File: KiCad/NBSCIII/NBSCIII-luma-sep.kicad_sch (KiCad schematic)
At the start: 11 parts, among them U1 LM324N

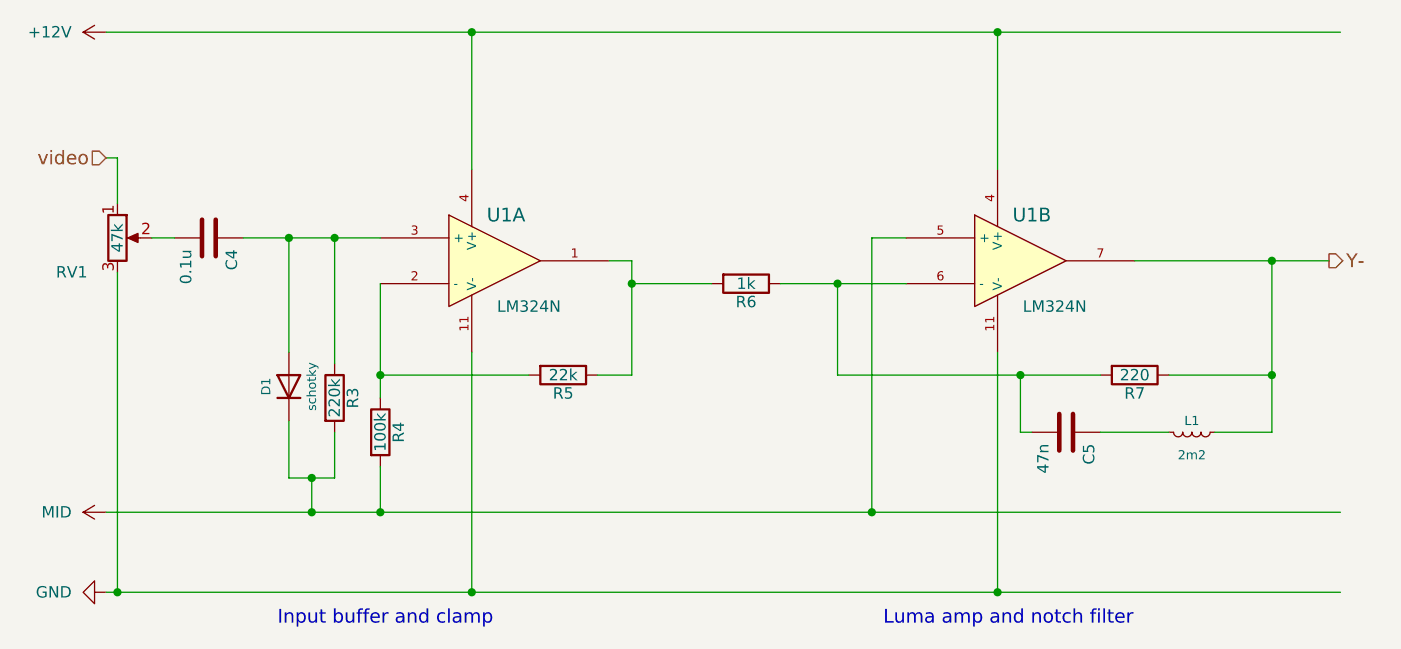
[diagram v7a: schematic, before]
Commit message: derescue lm324
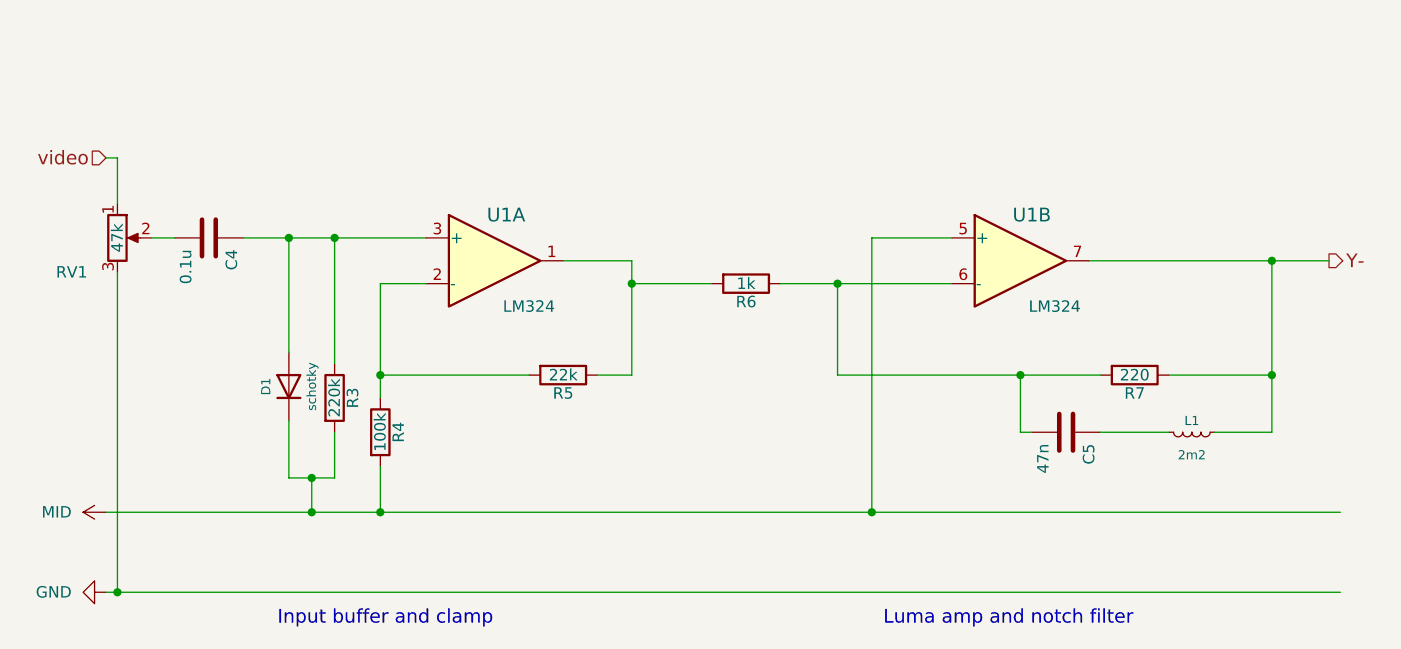
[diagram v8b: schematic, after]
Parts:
- U1: value LM324N -> LM324; symbol NBSCIII-rescue:LM324N -> Amplifier_Operational:LM324
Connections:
- net GND: no longer U1.11 (V-), U1.11 (V-)
- removed net +12V: U1.4 (V+), U1.4 (V+)
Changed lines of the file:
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@@
   (junction (at 68.58 59.69) (diameter 0) (color 0 0 0 0)
   )
-  (junction (at 142.24 36.83) (diameter 0) (color 0 0 0 0)
-  )
-  (junction (at 83.82 36.83) (diameter 0) (color 0 0 0 0)
-  )
   (junction (at 63.5 59.69) (diameter 0) (color 0 0 0 0)
   )
-  (junction (at 142.24 99.06) (diameter 0) (color 0 0 0 0)
-  )
-  (junction (at 83.82 99.06) (diameter 0) (color 0 0 0 0)
-  )
   (junction (at 66.04 90.17) (diameter 0) (color 0 0 0 0)
   )
@@
   (junction (at 66.04 86.36) (diameter 0) (color 0 0 0 0)
   )
-  (wire (pts (xy 128.27 59.69) (xy 132.08 59.69))
+  (wire (pts (xy 128.27 59.69) (xy 137.16 59.69))
     (stroke (width 0) (type default) (color 0 0 0 0))
   )
@@
     (stroke (width 0) (type default) (color 0 0 0 0))
   )
-  (wire (pts (xy 83.82 99.06) (xy 142.24 99.06))
-    (stroke (width 0) (type default) (color 0 0 0 0))
-  )
   (wire (pts (xy 68.58 59.69) (xy 68.58 73.66))
     (stroke (width 0) (type default) (color 0 0 0 0))
@@
     (stroke (width 0) (type default) (color 0 0 0 0))
   )
-  (wire (pts (xy 142.24 36.83) (xy 142.24 52.07))
-    (stroke (width 0) (type default) (color 0 0 0 0))
-  )
   (wire (pts (xy 73.66 74.93) (xy 73.66 77.47))
     (stroke (width 0) (type default) (color 0 0 0 0))
@@
     (stroke (width 0) (type default) (color 0 0 0 0))
   )
-  (wire (pts (xy 83.82 36.83) (xy 142.24 36.83))
-    (stroke (width 0) (type default) (color 0 0 0 0))
-  )
   (wire (pts (xy 128.27 90.17) (xy 128.27 59.69))
     (stroke (width 0) (type default) (color 0 0 0 0))
   )
-  (wire (pts (xy 142.24 99.06) (xy 180.34 99.06))
-    (stroke (width 0) (type default) (color 0 0 0 0))
-  )
-  (wire (pts (xy 44.45 99.06) (xy 83.82 99.06))
+  (wire (pts (xy 44.45 99.06) (xy 180.34 99.06))
     (stroke (width 0) (type default) (color 0 0 0 0))
   )
@@
     (stroke (width 0) (type default) (color 0 0 0 0))
   )
-  (wire (pts (xy 142.24 99.06) (xy 142.24 72.39))
-    (stroke (width 0) (type default) (color 0 0 0 0))
-  )
   (wire (pts (xy 63.5 59.69) (xy 68.58 59.69))
     (stroke (width 0) (type default) (color 0 0 0 0))
   )
-  (wire (pts (xy 83.82 52.07) (xy 83.82 36.83))
+  (wire (pts (xy 73.66 64.77) (xy 78.74 64.77))
     (stroke (width 0) (type default) (color 0 0 0 0))
   )
@@
     (stroke (width 0) (type default) (color 0 0 0 0))
   )
-  (wire (pts (xy 43.18 36.83) (xy 83.82 36.83))
-    (stroke (width 0) (type default) (color 0 0 0 0))
-  )
   (wire (pts (xy 101.6 64.77) (xy 101.6 74.93))
     (stroke (width 0) (type default) (color 0 0 0 0))
   )
-  (wire (pts (xy 157.48 62.23) (xy 172.72 62.23))
-    (stroke (width 0) (type default) (color 0 0 0 0))
-  )
   (wire (pts (xy 144.78 74.93) (xy 153.67 74.93))
     (stroke (width 0) (type default) (color 0 0 0 0))
@@
     (stroke (width 0) (type default) (color 0 0 0 0))
   )
-  (wire (pts (xy 142.24 36.83) (xy 180.34 36.83))
-    (stroke (width 0) (type default) (color 0 0 0 0))
-  )
   (wire (pts (xy 144.78 81.28) (xy 146.05 81.28))
     (stroke (width 0) (type default) (color 0 0 0 0))
@@
     (stroke (width 0) (type default) (color 0 0 0 0))
   )
-  (wire (pts (xy 68.58 59.69) (xy 73.66 59.69))
+  (wire (pts (xy 68.58 59.69) (xy 78.74 59.69))
+    (stroke (width 0) (type default) (color 0 0 0 0))
+  )
+  (wire (pts (xy 124.46 64.77) (xy 137.16 64.77))
     (stroke (width 0) (type default) (color 0 0 0 0))
   )
@@
     (stroke (width 0) (type default) (color 0 0 0 0))
   )
+  (wire (pts (xy 152.4 62.23) (xy 172.72 62.23))
+    (stroke (width 0) (type default) (color 0 0 0 0))
+  )
   (wire (pts (xy 172.72 81.28) (xy 172.72 74.93))
     (stroke (width 0) (type default) (color 0 0 0 0))
@@
     (stroke (width 0) (type default) (color 0 0 0 0))
   )
-  (wire (pts (xy 132.08 64.77) (xy 124.46 64.77))
-    (stroke (width 0) (type default) (color 0 0 0 0))
-  )
   (wire (pts (xy 144.78 81.28) (xy 144.78 74.93))
     (stroke (width 0) (type default) (color 0 0 0 0))
@@
     (stroke (width 0) (type default) (color 0 0 0 0))
   )
-  (wire (pts (xy 83.82 72.39) (xy 83.82 99.06))
-    (stroke (width 0) (type default) (color 0 0 0 0))
-  )
   (wire (pts (xy 172.72 74.93) (xy 172.72 62.23))
     (stroke (width 0) (type default) (color 0 0 0 0))
@@
     (stroke (width 0) (type default) (color 0 0 0 0))
   )
-  (wire (pts (xy 99.06 62.23) (xy 101.6 62.23))
+  (wire (pts (xy 93.98 62.23) (xy 101.6 62.23))
     (stroke (width 0) (type default) (color 0 0 0 0))
   )
@@
     (effects (font (size 1.524 1.524)) (justify left))
   )
-  (symbol (lib_id "NBSCIII-rescue:LM324N") (at 86.36 62.23 0) (unit 1)
+  (symbol (lib_id "Amplifier_Operational:LM324") (at 86.36 62.23 0) (unit 1)
     (in_bom yes) (on_board yes)
     (property "Reference" "U1" (id 0) (at 87.63 57.15 0)
       (effects (font (size 1.524 1.524)))
     )
-    (property "Value" "LM324N" (id 1) (at 90.17 67.31 0))
+    (property "Value" "LM324" (id 1) (at 90.17 67.31 0))
     (property "Footprint" "" (id 2) (at 86.36 62.23 0)
       (effects (font (size 1.27 1.27)) hide)
@@
       (effects (font (size 1.27 1.27)) hide)
     )
-    (pin "11")
-    (pin "4")
     (pin "1")
     (pin "2")
@@
     (pin "13")
     (pin "14")
+    (pin "11")
+    (pin "4")
   )
   (symbol (lib_id "Device:R_Potentiometer") (at 44.45 59.69 0) (unit 1)
@@
     (pin "2")
   )
-  (symbol (lib_id "NBSCIII-rescue:LM324N") (at 144.78 62.23 0) (unit 2)
+  (symbol (lib_id "Amplifier_Operational:LM324") (at 144.78 62.23 0) (unit 2)
     (in_bom yes) (on_board yes)
     (property "Reference" "U1" (id 0) (at 146.05 57.15 0)
       (effects (font (size 1.524 1.524)))
     )
-    (property "Value" "LM324N" (id 1) (at 148.59 67.31 0))
+    (property "Value" "LM324" (id 1) (at 148.59 67.31 0))
     (property "Footprint" "" (id 2) (at 144.78 62.23 0)
       (effects (font (size 1.27 1.27)) hide)
@@
       (effects (font (size 1.27 1.27)) hide)
     )
-    (pin "11")
-    (pin "4")
     (pin "1")
     (pin "2")
@@
     (pin "13")
     (pin "14")
+    (pin "11")
+    (pin "4")
   )
   (symbol (lib_id "Device:R") (at 114.3 64.77 270) (unit 1)
@@
       (effects (font (size 1.27 1.27)) hide)
     )
-    (pin "1")
-  )
-  (symbol (lib_id "power:+12V") (at 43.18 36.83 90) (unit 1)
-    (in_bom yes) (on_board yes) (fields_autoplaced)
-    (property "Reference" "#PWR0104" (id 0) (at 46.99 36.83 0)
-      (effects (font (size 1.27 1.27)) hide)
-    )
-    (property "Value" "+12V" (id 1) (at 39.37 36.8299 90)
-      (effects (font (size 1.27 1.27)) (justify left))
-    )
-    (property "Footprint" "" (id 2) (at 43.18 36.83 0)
-      (effects (font (size 1.27 1.27)) hide)
-    )
-    (property "Datasheet" "" (id 3) (at 43.18 36.83 0)
-      (effects (font (size 1.27 1.27)) hide)
-    )
